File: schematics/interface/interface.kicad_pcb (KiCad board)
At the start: 2 copper layers, 100 x 91 mm, 18 parts, among them U1 74LS00, U2 74LS00, U4 74LS245, U5 74LS193, U6 74LS193, U7 74LS193, U8 74LS193

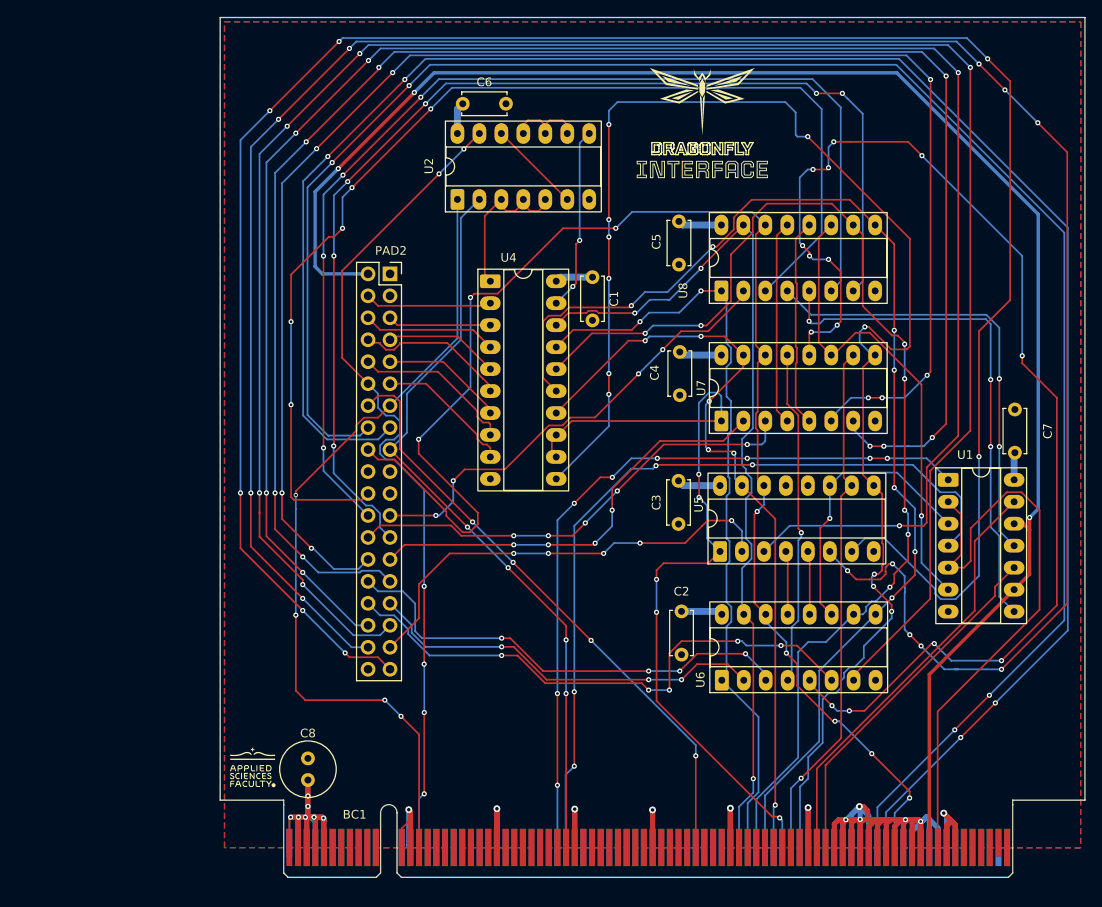
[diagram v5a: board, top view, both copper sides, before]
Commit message: fix(alu, interface): fix tp
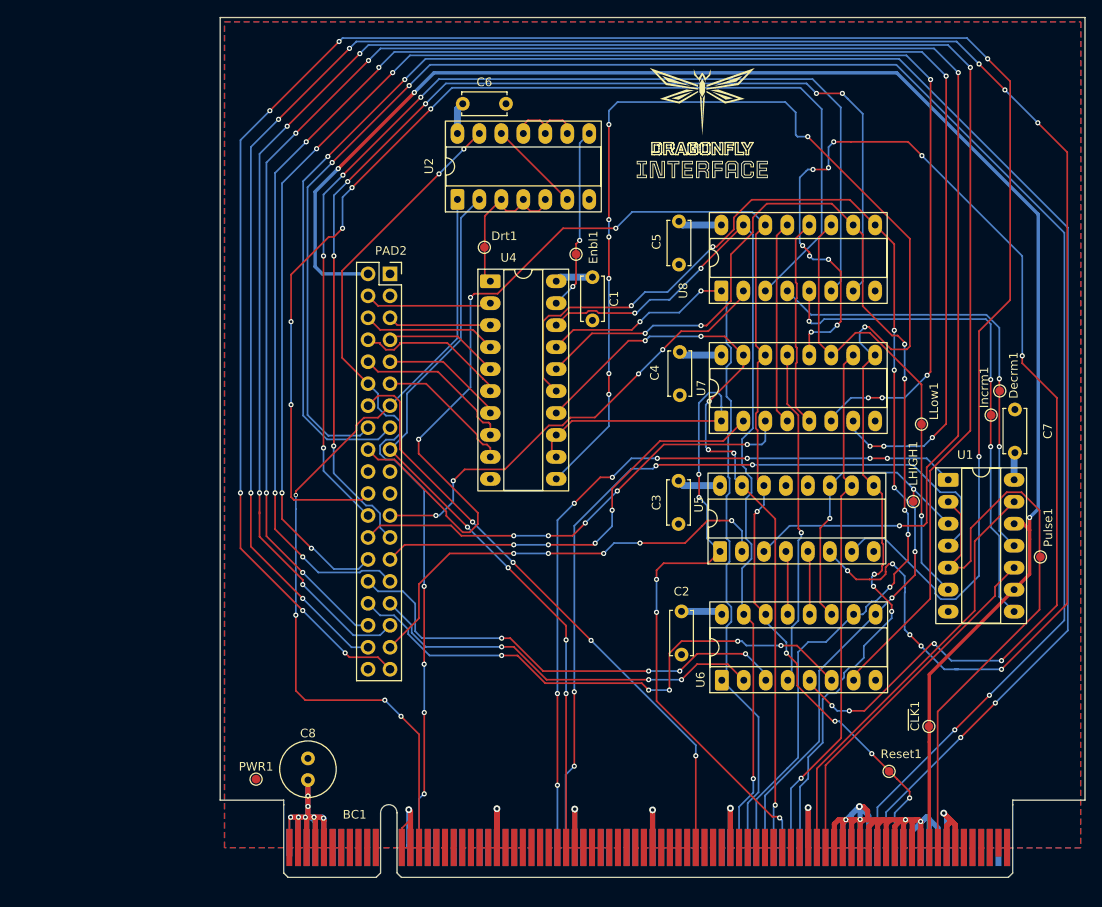
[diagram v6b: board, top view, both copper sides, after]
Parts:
- added Decrm1: Decrement, TestPoint:TestPoint_Pad_D1.0mm, F.Cu at (175.8, 65.8)
- added Drt1: Direction, TestPoint:TestPoint_Pad_D1.0mm, F.Cu at (116.2, 49.2)
- added Enbl1: Enable, TestPoint:TestPoint_Pad_D1.0mm, F.Cu at (126.8, 50.0)
- added Incrm1: Increment, TestPoint:TestPoint_Pad_D1.0mm, F.Cu at (174.8, 68.6)
- added LHIGH1: LoadHigh, TestPoint:TestPoint_Pad_D1.0mm, F.Cu at (165.8, 78.6)
- added LLow1: LoadLow, TestPoint:TestPoint_Pad_D1.0mm, F.Cu at (166.8, 69.7)
- added PWR1: Power, TestPoint:TestPoint_Pad_D1.0mm, F.Cu at (89.8, 110.7)
- added Pulse1: Pulse, TestPoint:TestPoint_Pad_D1.0mm, F.Cu at (180.5, 85.0)
- added Reset1: Reset, TestPoint:TestPoint_Pad_D1.0mm, F.Cu at (163.0, 109.8)
- added ~{CLK}1: ~{Clock}, TestPoint:TestPoint_Pad_D1.0mm, F.Cu at (167.6, 104.6)
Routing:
- net Net-(U5-~{LOAD}): track 32.7 -> 34.2 mm, vias 1 -> 2

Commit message: done
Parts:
- added kibuzzard-691DE158: G***, kibuzzard-691DE158, F.Cu at (182.0, 104.5)
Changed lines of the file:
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@@
+		(embedded_fonts no)
+	)
+	(footprint "kibuzzard-691DE158"
+		(layer "F.Cu")
+		(at 182 104.5 90)
+		(descr "Generated with KiBuzzard")
+		(tags "kb_params=eyJBbGlnbm1lbnRDaG9pY2UiOiAiQ2VudGVyIiwgIkNhcExlZnRDaG9pY2UiOiAiIiwgIkNhcFJpZ2h0Q2hvaWNlIjogIi8iLCAiRm9udENvbWJvQm94IjogIlRvdXJuZXktUmVndWxhciIsICJIZWlnaHRDdHJsIjogMi4wLCAiTGF5ZXJDb21ib0JveCI6ICJGLlNpbGtTIiwgIkxpbmVTcGFjaW5nQ3RybCI6IDEuNSwgIk11bHRpTGluZVRleHQiOiAiVUNVIEFQUFMuIiwgIlBhZGRpbmdCb3R0b21DdHJsIjogNS4wLCAiUGFkZGluZ0xlZnRDdHJsIjogNS4wLCAiUGFkZGluZ1JpZ2h0Q3RybCI6IDUuMCwgIlBhZGRpbmdUb3BDdHJsIjogNS4wLCAiV2lkdGhDdHJsIjogMS4wLCAiYWR2YW5jZWRDaGVja2JveCI6IHRydWUsICJpbmxpbmVGb3JtYXRUZXh0Ym94IjogdHJ1ZSwgImxpbmVvdmVyU3R5bGVDaG9pY2UiOiAiU3F1YXJlIiwgImxpbmVvdmVyVGhpY2tuZXNzQ3RybCI6IDF9")
+		(property "Reference" "kibuzzard-691DE158"
+			(at 0 -4.048 90)
+			(layer "F.SilkS")
+			(hide yes)
+			(effects
+				(font
+					(size 0.001 0.001)
+					(thickness 0.15)
+				)
+			)
+		)
+		(property "Value" "G***"
+			(at 0 4.048 90)
+			(layer "F.SilkS")
+			(hide yes)
+			(effects
+				(font
+					(size 0.001 0.001)
+					(thickness 0.15)
+				)
+			)
+		)
+		(property "Datasheet" ""
+			(at 0 0 90)
+			(layer "F.Fab")
+			(hide yes)
+			(effects
+				(font
+					(size 1.27 1.27)
+					(thickness 0.15)
+				)
+			)
+		)
+		(property "Description" ""
+			(at 0 0 90)
+			(layer "F.Fab")
+			(hide yes)
+			(effects
+				(font
+					(size 1.27 1.27)
+					(thickness 0.15)
+				)
+			)
+		)
+		(attr board_only exclude_from_pos_files exclude_from_bom)
+		(fp_poly
+			(pts
+				(xy 6.606429 1) (xy 6.606429 0.58) (xy 7.055 0.58) (xy 7.055 1) (xy 6.722143 1) (xy 6.722143 0.885714)
+				(xy 6.940714 0.885714) (xy 6.940714 0.692857) (xy 6.722143 0.692857) (xy 6.722143 0.885714) (xy 6.722143 1)
+				(xy 6.606429 1)
+			)
+			(stroke
+				(width 0)
+				(type solid)
+			)
+			(fill yes)
+			(layer "F.SilkS")
+		)
+		(fp_poly
+			(pts
+				(xy 3.246429 0.105714) (xy 3.246429 -0.708571) (xy 4.002143 -0.708571) (xy 4.146429 -0.565714) (xy 4.146429 -0.064286)
+				(xy 3.975 0.105714) (xy 3.357857 0.105714) (xy 3.357857 -0.001429) (xy 3.916429 -0.001429) (xy 4.032143 -0.115714)
+				(xy 4.032143 -0.508571) (xy 3.945 -0.595714) (xy 3.357857 -0.595714) (xy 3.357857 -0.001429) (xy 3.357857 0.105714)
+				(xy 3.246429 0.105714)
+			)
+			(stroke
+				(width 0)
+				(type solid)
+			)
+			(fill yes)
+			(layer "F.SilkS")
+		)
+		(fp_poly
+			(pts
+				(xy 1.449286 0.105714) (xy 1.449286 -0.708571) (xy 2.205 -0.708571) (xy 2.349286 -0.565714) (xy 2.349286 -0.064286)
+				(xy 2.177857 0.105714) (xy 1.560714 0.105714) (xy 1.560714 -0.001429) (xy 2.119286 -0.001429) (xy 2.235 -0.115714)
+				(xy 2.235 -0.508571) (xy 2.147857 -0.595714) (xy 1.560714 -0.595714) (xy 1.560714 -0.001429) (xy 1.560714 0.105714)
+				(xy 1.449286 0.105714)
+			)
+			(stroke
+				(width 0)
+				(type solid)
+			)
+			(fill yes)
+			(layer "F.SilkS")
+		)
+		(fp_poly
+			(pts
+				(xy -0.400714 0.12) (xy -0.400714 -0.568571) (xy -0.256429 -0.712857) (xy 0.376429 -0.712857) (xy 0.520714 -0.568571)
+				(xy 0.520714 0.12) (xy -0.295 0.12) (xy -0.295 0.008571) (xy 0.410714 0.008571) (xy 0.410714 -0.508571)
+				(xy 0.323571 -0.595714) (xy -0.207857 -0.595714) (xy -0.295 -0.508571) (xy -0.295 0.008571) (xy -0.295 0.12)
+				(xy -0.400714 0.12)
+			)
+			(stroke
+				(width 0)
+				(type solid)
+			)
+			(fill yes)
+			(layer "F.SilkS")
+		)
+		(fp_poly
+			(pts
+				(xy 2.953571 1) (xy 2.953571 -1) (xy 4.140714 -1) (xy 4.435 -0.705714) (xy 4.435 0.081429) (xy 4.113571 0.402857)
+				(xy 3.357857 0.402857) (xy 3.357857 1) (xy 3.062143 1) (xy 3.062143 0.902857) (xy 3.246429 0.902857)
+				(xy 3.246429 0.288571) (xy 4.065 0.288571) (xy 4.329286 0.022857) (xy 4.329286 -0.654286) (xy 4.090714 -0.892857)
+				(xy 3.062143 -0.892857) (xy 3.062143 0.902857) (xy 3.062143 1) (xy 2.953571 1)
+			)
+			(stroke
+				(width 0)
+				(type solid)
+			)
+			(fill yes)
+			(layer "F.SilkS")
+		)
+		(fp_poly
+			(pts
+				(xy 1.156429 1) (xy 1.156429 -1) (xy 2.343571 -1) (xy 2.637857 -0.705714) (xy 2.637857 0.081429)
+				(xy 2.316429 0.402857) (xy 1.560714 0.402857) (xy 1.560714 1) (xy 1.265 1) (xy 1.265 0.902857) (xy 1.449286 0.902857)
+				(xy 1.449286 0.288571) (xy 2.267857 0.288571) (xy 2.532143 0.022857) (xy 2.532143 -0.654286) (xy 2.293571 -0.892857)
+				(xy 1.265 -0.892857) (xy 1.265 0.902857) (xy 1.265 1) (xy 1.156429 1)
+			)
+			(stroke
+				(width 0)
+				(type solid)
+			)
+			(fill yes)
+			(layer "F.SilkS")
+		)
+		(fp_poly
+			(pts
+				(xy -0.697857 1) (xy -0.697857 -0.705714) (xy -0.403571 -1) (xy 0.519286 -1) (xy 0.813571 -0.705714)
+				(xy 0.813571 1) (xy 0.410714 1) (xy 0.410714 0.411429) (xy -0.295 0.411429) (xy -0.295 1) (xy -0.583571 1)
+				(xy -0.583571 0.881429) (xy -0.400714 0.881429) (xy -0.400714 0.304286) (xy 0.520714 0.304286) (xy 0.520714 0.881429)
+				(xy 0.705 0.881429) (xy 0.705 -0.657143) (xy 0.465 -0.895714) (xy -0.345 -0.895714) (xy -0.583571 -0.657143)
+				(xy -0.583571 0.881429) (xy -0.583571 1) (xy -0.697857 1)
+			)
+			(stroke
+				(width 0)
+				(type solid)
+			)
+			(fill yes)
+			(layer "F.SilkS")
+		)
+		(fp_poly
+			(pts
+				(xy -3.086429 1) (xy -3.380714 0.705714) (xy -3.380714 -1) (xy -2.976429 -1) (xy -2.976429 0.508571)
+				(xy -2.889286 0.595714) (xy -2.303571 0.595714) (xy -2.216429 0.508571) (xy -2.216429 -1) (xy -1.812143 -1)
+				(xy -1.812143 0.705714) (xy -2.106429 1) (xy -3.030714 1) (xy -3.030714 0.89) (xy -2.160714 0.89)
+				(xy -1.922143 0.652857) (xy -1.922143 -0.892857) (xy -2.105 -0.892857) (xy -2.105 0.564286) (xy -2.250714 0.705714)
+				(xy -2.940714 0.705714) (xy -3.086429 0.564286) (xy -3.086429 -0.892857) (xy -3.270714 -0.892857)
+				(xy -3.270714 0.652857) (xy -3.030714 0.89) (xy -3.030714 1) (xy -3.086429 1)
+			)
+			(stroke
+				(width 0)
+				(type solid)
+			)
+			(fill yes)
+			(layer "F.SilkS")
+		)
+		(fp_poly
+			(pts
+				(xy -6.760714 1) (xy -7.055 0.705714) (xy -7.055 -1) (xy -6.650714 -1) (xy -6.650714 0.508571) (xy -6.563571 0.595714)
+				(xy -5.977857 0.595714) (xy -5.890714 0.508571) (xy -5.890714 -1) (xy -5.486429 -1) (xy -5.486429 0.705714)
+				(xy -5.780714 1) (xy -6.705 1) (xy -6.705 0.89) (xy -5.835 0.89) (xy -5.596429 0.652857) (xy -5.596429 -0.892857)
+				(xy -5.779286 -0.892857) (xy -5.779286 0.564286) (xy -5.925 0.705714) (xy -6.615 0.705714) (xy -6.760714 0.564286)
+				(xy -6.760714 -0.892857) (xy -6.945 -0.892857) (xy -6.945 0.652857) (xy -6.705 0.89) (xy -6.705 1)
+				(xy -6.760714 1)
+			)
+			(stroke
+				(width 0)
+				(type solid)
+			)
+			(fill yes)
+			(layer "F.SilkS")
+		)
+		(fp_poly
+			(pts
+				(xy -4.877857 1) (xy -5.172143 0.705714) (xy -5.172143 -0.705714) (xy -4.877857 -1) (xy -3.990714 -1)
+				(xy -3.695 -0.705714) (xy -3.695 -0.245714) (xy -4.099286 -0.245714) (xy -4.099286 -0.508571) (xy -4.186429 -0.595714)
+				(xy -4.680714 -0.595714) (xy -4.767857 -0.508571) (xy -4.767857 0.508571) (xy -4.680714 0.595714)
+				(xy -4.186429 0.595714) (xy -4.099286 0.508571) (xy -4.099286 0.245714) (xy -3.695 0.245714) (xy -3.695 0.705714)
+				(xy -3.990714 1) (xy -4.823571 1) (xy -4.823571 0.888571) (xy -4.043571 0.888571) (xy -3.805 0.65)
+				(xy -3.805 0.344286) (xy -3.987857 0.344286) (xy -3.987857 0.561429) (xy -4.133571 0.705714) (xy -4.733571 0.705714)
+				(xy -4.879286 0.561429) (xy -4.879286 -0.565714) (xy -4.733571 -0.708571) (xy -4.133571 -0.708571)
+				(xy -3.987857 -0.565714) (xy -3.987857 -0.348571) (xy -3.805 -0.348571) (xy -3.805 -0.654286) (xy -4.043571 -0.892857)
+				(xy -4.823571 -0.892857) (xy -5.062143 -0.654286) (xy -5.062143 0.65) (xy -4.823571 0.888571) (xy -4.823571 1)
+				(xy -4.877857 1)
+			)
+			(stroke
+				(width 0)
+				(type solid)
+			)
+			(fill yes)
+			(layer "F.SilkS")
+		)
+		(fp_poly
+			(pts
+				(xy 5.030714 1) (xy 4.736429 0.705714) (xy 4.736429 0.345714) (xy 5.140714 0.345714) (xy 5.140714 0.508571)
+				(xy 5.227857 0.595714) (xy 5.776429 0.595714) (xy 5.863571 0.508571) (xy 5.863571 0.288571) (xy 5.776429 0.201429)
+				(xy 5.039286 0.201429) (xy 4.745 -0.092857) (xy 4.745 -0.705714) (xy 5.039286 -1) (xy 5.946429 -1)
+				(xy 6.240714 -0.705714) (xy 6.240714 -0.345714) (xy 5.836429 -0.345714) (xy 5.836429 -0.508571)
+				(xy 5.749286 -0.595714) (xy 5.236429 -0.595714) (xy 5.147857 -0.508571) (xy 5.147857 -0.29) (xy 5.236429 -0.202857)
+				(xy 5.973571 -0.202857) (xy 6.267857 0.091429) (xy 6.267857 0.705714) (xy 5.973571 1) (xy 5.082143 1)
+				(xy 5.082143 0.89) (xy 5.915 0.89) (xy 6.153571 0.651429) (xy 6.153571 0.131429) (xy 5.929286 -0.094286)
+				(xy 5.185 -0.094286) (xy 5.039286 -0.238571) (xy 5.039286 -0.562857) (xy 5.183571 -0.705714) (xy 5.807857 -0.705714)
+				(xy 5.946429 -0.57) (xy 5.946429 -0.447143) (xy 6.129286 -0.447143) (xy 6.129286 -0.658571) (xy 5.897857 -0.89)
+				(xy 5.093571 -0.89) (xy 4.855 -0.651429) (xy 4.855 -0.151429) (xy 5.096429 0.091429) (xy 5.839286 0.091429)
+				(xy 5.969286 0.217143) (xy 5.969286 0.562857) (xy 5.825 0.707143) (xy 5.172143 0.707143) (xy 5.035 0.57)
+				(xy 5.035 0.447143) (xy 4.850714 0.447143) (xy 4.850714 0.658571) (xy 5.082143 0.89) (xy 5.082143 1)
+				(xy 5.030714 1)
+			)
+			(stroke
+				(width 0)
+				(type solid)
+			)
+			(fill yes)
+			(layer "F.SilkS")
+		)
 		(embedded_fonts no)
 	)
